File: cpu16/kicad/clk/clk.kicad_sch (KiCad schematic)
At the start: 34 parts, among them J3 BACKPLANE_2x32, SW1 SW_PUSH, SW2 SW_PUSH, SW3 SW_SPDT, SW4 SW_SPDT, U121 74HC14, U122 74HC157, U123 74HC175, U124 74HC74, U125 74HC74, U126 74HC541, U138 74HC08, U143 74HC32, U162 74HC04, X1 OSC_CAN

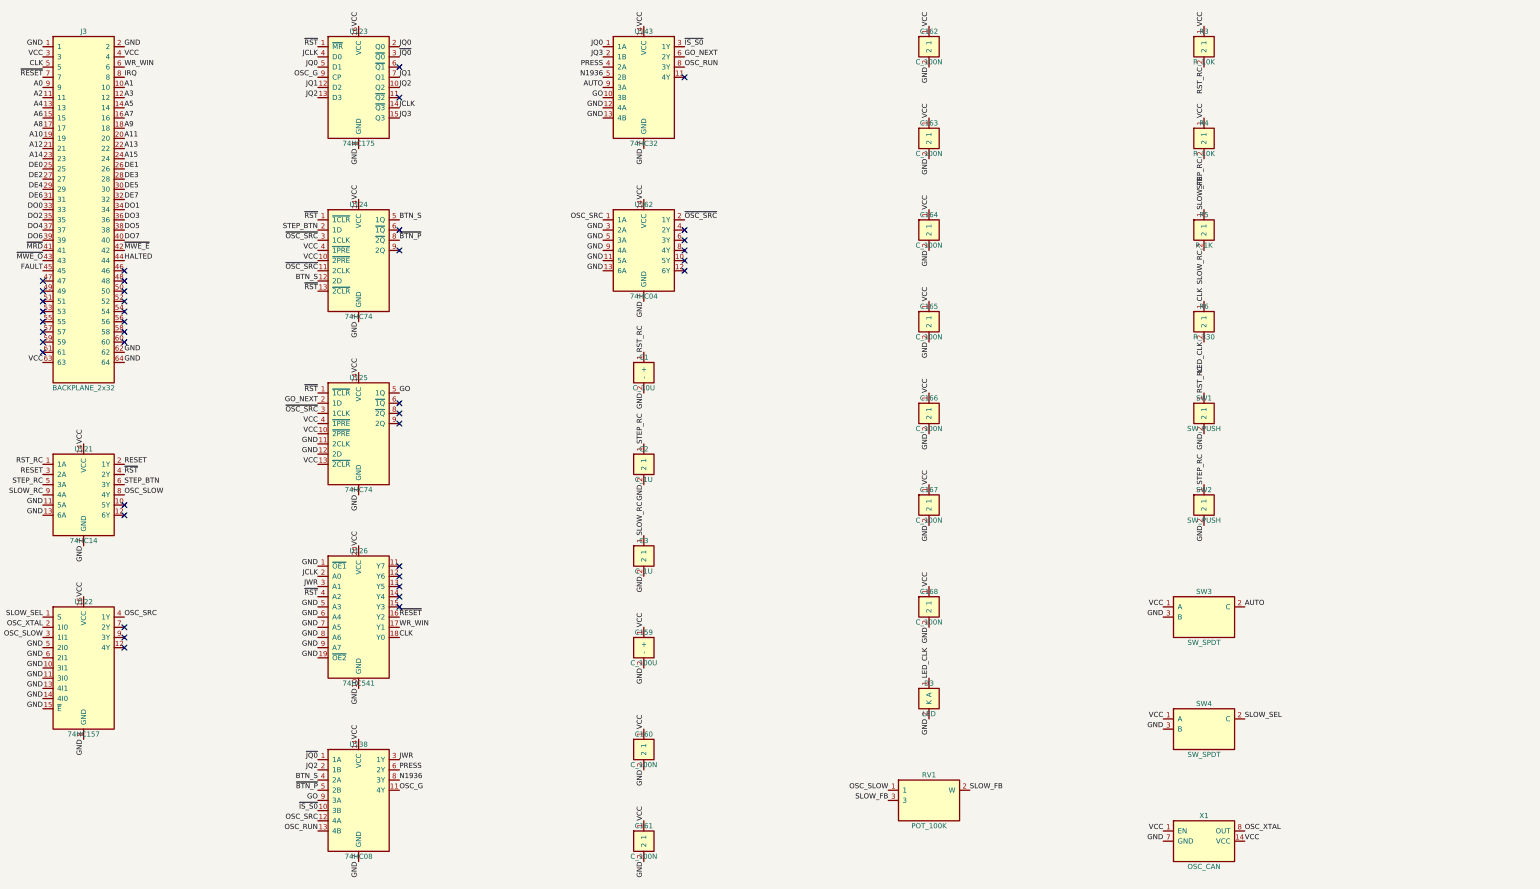
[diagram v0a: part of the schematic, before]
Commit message: Kart başına kararlı referans numaraları; yapıştırıcı kapı ve pasiflerde blok bilgisi
Her kart kendi KiCad projesi olduğu için numaralar kart içinde verilir (cpu U1.., clk U201..,
mem U301..). Deney rehberi bir bloğun hangi kapı birimlerini kullandığını bilsin diye yapıştırıcı
lojik çiplerine birim → blok eşlemesi eklendi.

Co-Authored-By: Claude Opus 5.5 (1M context) <noreply@anthropic.com>
Claude-Session: https://claude.ai/code/session_018J8WVuECVRbQJyCbmF6Nsi
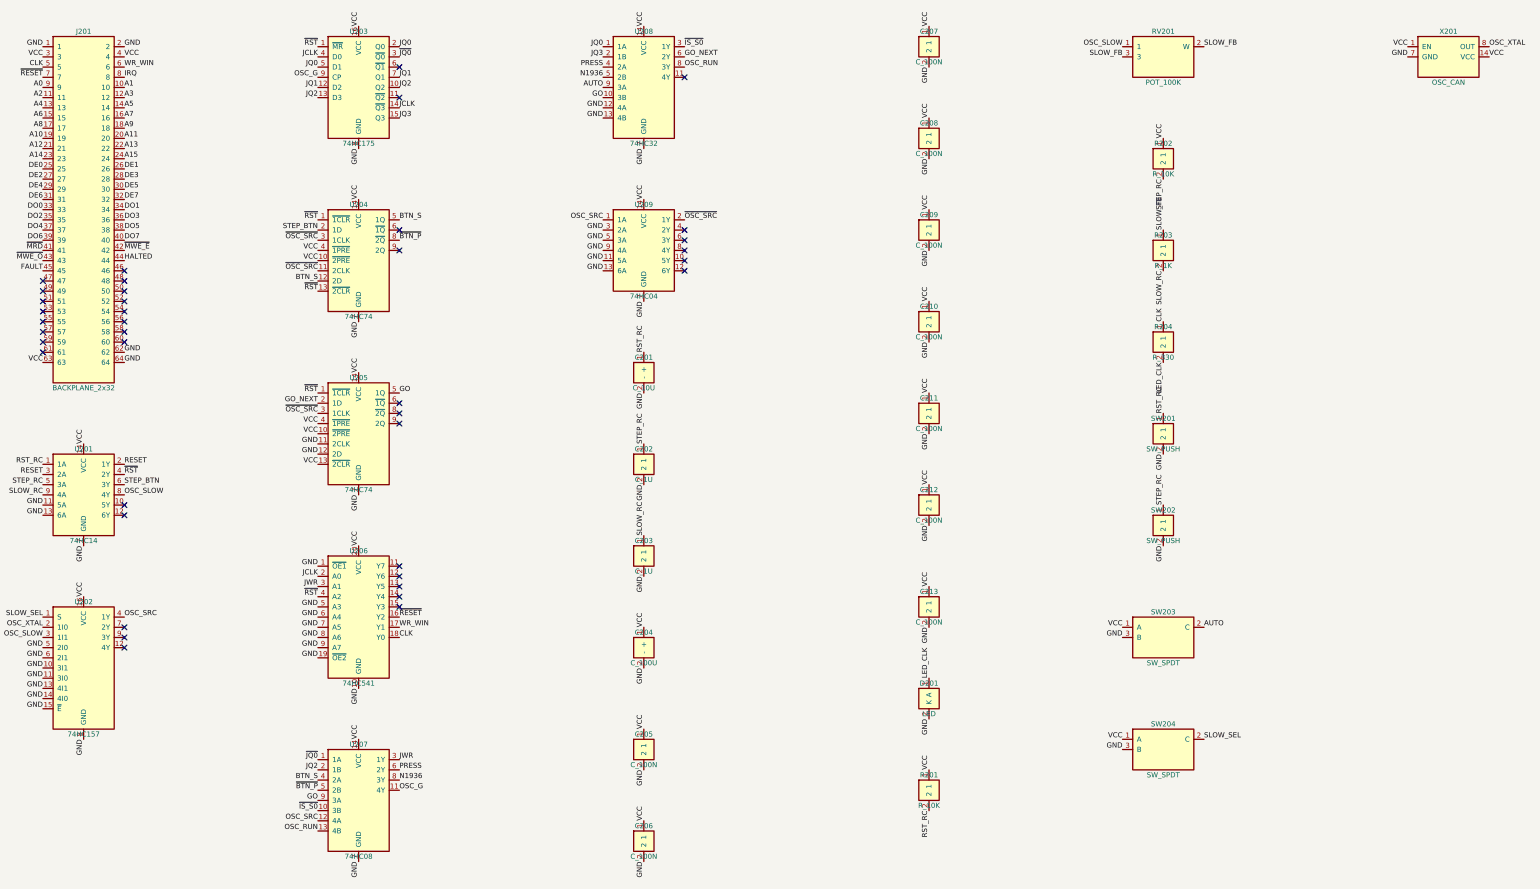
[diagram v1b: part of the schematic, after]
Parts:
- removed R3: R_10K, Resistor_THT:R_Axial_DIN0207_L6.3mm_D2.5mm_P7.62mm_Horizontal, symbol cpu16:R_10K
- removed RV1: POT_100K, Potentiometer_THT:Potentiometer_Bourns_3386P_Vertical, symbol cpu16:POT_100K
- added R201: R_10K, Resistor_THT:R_Axial_DIN0207_L6.3mm_D2.5mm_P7.62mm_Horizontal, symbol cpu16:R_10K
- added RV201: POT_100K, Potentiometer_THT:Potentiometer_Bourns_3386P_Vertical, symbol cpu16:POT_100K
- C205: renamed from C160; Gorev U121 dekuplaj -> U201 dekuplaj
- C206: renamed from C161; Gorev U122 dekuplaj -> U202 dekuplaj
- C207: renamed from C162; Gorev U123 dekuplaj -> U203 dekuplaj
- C208: renamed from C163; Gorev U124 dekuplaj -> U204 dekuplaj
- C209: renamed from C164; Gorev U125 dekuplaj -> U205 dekuplaj
- C210: renamed from C165; Gorev U126 dekuplaj -> U206 dekuplaj
- C211: renamed from C166; Gorev U138 dekuplaj -> U207 dekuplaj
- C212: renamed from C167; Gorev U143 dekuplaj -> U208 dekuplaj
- C213: renamed from C168; Gorev U162 dekuplaj -> U209 dekuplaj
- renumbered C1 to C201, C2 to C202, C3 to C203, C159 to C204, D3 to D201, J3 to J201, R4 to R202, R5 to R203, R6 to R204, SW1 to SW201, SW2 to SW202, SW3 to SW203, SW4 to SW204, U121 to U201, U122 to U202, U123 to U203, U124 to U204, U125 to U205, U126 to U206, U138 to U207, U143 to U208, U162 to U209, X1 to X201
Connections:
- net OSC_SLOW: now also RV201.1
- net RST_RC: now also R201.2
- net SLOW_FB: now also RV201.2 (W), RV201.3
- net VCC: now also R201.1
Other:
- moved on the sheet: R202, R203, R204, SW201, SW202, SW203, SW204, X201

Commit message: Faz 9: şemadan statik zamanlama analizi; C/V bayrak saati düzeltmesi
- board/zamanlama.ts: saat ağacı, flip-flop'tan flip-flop'a en uzun yollar, yarım/tam periyot,
  kapılı saat kurulum ve tutma kontrolleri; 74HC veri sayfası gecikmeleri (tip / maks) ve yük
  düzeltmesi. npm run cpu16 -- zamanlama [--tip]
- Sonuç: en kötü durumda CPU 1,16 MHz, tipik 2,1 MHz; kritik yol kontrol register'ı → ALU ROM'u
  → 4 × 74HC283 → veriyolu (yarım periyot)
- Analizin bulduğu risk: C/V bayraklarının saat izni ALU ROM'unun SETSCV çıkışından geliyordu;
  ROM adresindeki CFLAG tam o kenarda değiştiği için ROM çıkışındaki bir sıçrama ikinci saat
  darbesi üretebilirdi. Artık dört bayrak aynı saatle yüklenir, SETSCV = 0 iken bir 74HC157
  eski C ve V'yi geri yazar (kapı seviyesi lockstep testleri geçiyor)
- Mikrokod testi: IR yüklenen adımda IR alanlarından seçilen register'a yazılmaz
- Deney rehberleri: otomatik bölümler yeniden üretildi; rehberlerin güncel olduğunu ve elle yazılan
  referansların şemada bulunduğunu denetleyen testler
- KiCad şemaları ve BOM yeniden üretildi

Co-Authored-By: Claude Opus 5.5 (1M context) <noreply@anthropic.com>
Claude-Session: https://claude.ai/code/session_018J8WVuECVRbQJyCbmF6Nsi
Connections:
- net N1936 renamed N1947
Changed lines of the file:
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@@
   (label "JWR" (at 134.62 231.14 0) (fields_autoplaced) (effects (font (size 1.27 1.27)) (justify left bottom)))
   (label "PRESS" (at 134.62 233.68 0) (fields_autoplaced) (effects (font (size 1.27 1.27)) (justify left bottom)))
-  (label "N1936" (at 134.62 236.22 0) (fields_autoplaced) (effects (font (size 1.27 1.27)) (justify left bottom)))
+  (label "N1947" (at 134.62 236.22 0) (fields_autoplaced) (effects (font (size 1.27 1.27)) (justify left bottom)))
   (label "OSC_G" (at 134.62 238.76 0) (fields_autoplaced) (effects (font (size 1.27 1.27)) (justify left bottom)))
   (label "GND" (at 124.46 256.54 270) (fields_autoplaced) (effects (font (size 1.27 1.27)) (justify right bottom)))
@@
   (label "JQ3" (at 185.42 55.88 180) (fields_autoplaced) (effects (font (size 1.27 1.27)) (justify right bottom)))
   (label "PRESS" (at 185.42 58.42 180) (fields_autoplaced) (effects (font (size 1.27 1.27)) (justify right bottom)))
-  (label "N1936" (at 185.42 60.96 180) (fields_autoplaced) (effects (font (size 1.27 1.27)) (justify right bottom)))
+  (label "N1947" (at 185.42 60.96 180) (fields_autoplaced) (effects (font (size 1.27 1.27)) (justify right bottom)))
   (label "AUTO" (at 185.42 63.5 180) (fields_autoplaced) (effects (font (size 1.27 1.27)) (justify right bottom)))
   (label "GO" (at 185.42 66.04 180) (fields_autoplaced) (effects (font (size 1.27 1.27)) (justify right bottom)))
